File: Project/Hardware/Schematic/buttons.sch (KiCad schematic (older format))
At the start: 0 parts

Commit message: Add files via upload (#6)
Switches inlagda och MicroUSB
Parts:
- added U7, U8: MomentSwitch, PASC:Momentswitch, symbol PASC:MomentSwitch
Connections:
- new net: U8.1 (IN1), U8.2 (IN2)
- new net: U8.3 (OUT1), U8.4 (OUT2)
- new net GND: U7.1 (IN1), U7.2 (IN2)
- new net NRST: U7.3 (OUT1), U7.4 (OUT2)
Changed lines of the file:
@@
 $Descr A4 11693 8268
 encoding utf-8
-Sheet 1 7
+Sheet 7 7
 Title ""
 Date ""
@@
 Comment4 ""
 $EndDescr
+$Comp
+L PASC:MomentSwitch U8
+U 1 1 5C5ECE12
+P 3800 2550
+F 0 "U8" H 3825 2975 50  0000 C CNN
+F 1 "MomentSwitch" H 3825 2884 50  0000 C CNN
+F 2 "PASC:Momentswitch" H 3800 2550 50  0001 C CNN
+F 3 "" H 3800 2550 50  0001 C CNN
+	1    3800 2550
+	1    0    0    -1
+$EndComp
+$Comp
+L PASC:MomentSwitch U7
+U 1 1 5C5ECEC3
+P 3800 1700
+F 0 "U7" H 3825 2125 50  0000 C CNN
+F 1 "MomentSwitch" H 3825 2034 50  0000 C CNN
+F 2 "PASC:Momentswitch" H 3800 1700 50  0001 C CNN
+F 3 "" H 3800 1700 50  0001 C CNN
+	1    3800 1700
+	1    0    0    -1
+$EndComp
+Wire Wire Line
+	3450 1500 3350 1500
+Wire Wire Line
+	3350 1500 3350 1700
+Wire Wire Line
+	3350 1900 3450 1900
+Wire Wire Line
+	3450 2350 3350 2350
+Wire Wire Line
+	3350 2350 3350 2750
+Wire Wire Line
+	3350 2750 3450 2750
+Wire Wire Line
+	4150 1500 4250 1500
+Wire Wire Line
+	4250 1500 4250 1700
+Wire Wire Line
+	4250 1900 4150 1900
+Wire Wire Line
+	4150 2350 4250 2350
+Wire Wire Line
+	4250 2350 4250 2750
+Wire Wire Line
+	4250 2750 4150 2750
+Wire Wire Line
+	4250 1700 4350 1700
+Connection ~ 4250 1700
+Wire Wire Line
+	4250 1700 4250 1900
+Text Label 4350 1700 0    50   ~ 0
+NRST
+Wire Wire Line
+	3350 1700 3250 1700
+Connection ~ 3350 1700
+Wire Wire Line
+	3350 1700 3350 1900
+$Comp
+L power:GND #PWR?
+U 1 1 5C5ED863
+P 3250 1700
+F 0 "#PWR?" H 3250 1450 50  0001 C CNN
+F 1 "GND" H 3255 1527 50  0000 C CNN
+F 2 "" H 3250 1700 50  0001 C CNN
+F 3 "" H 3250 1700 50  0001 C CNN
+	1    3250 1700
+	1    0    0    -1
+$EndComp
 $EndSCHEMATC

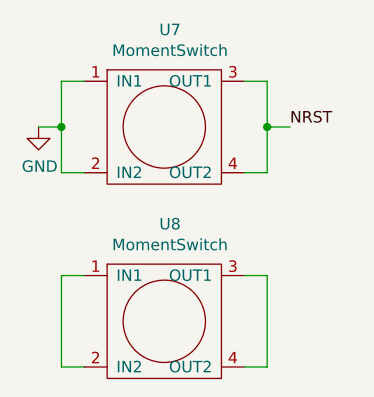
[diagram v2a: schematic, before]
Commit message: Pulse, piezo och labels (#8)
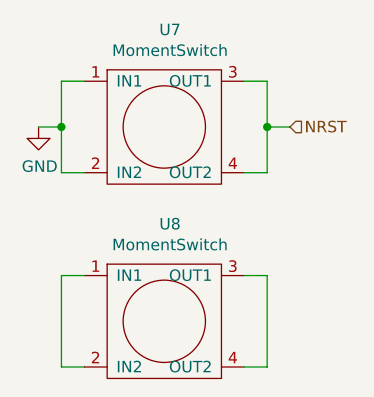
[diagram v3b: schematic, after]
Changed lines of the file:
@@
 Wire Wire Line
 	4250 1700 4250 1900
-Text Label 4350 1700 0    50   ~ 0
-NRST
 Wire Wire Line
 	3350 1700 3250 1700
@@
 	1    0    0    -1
 $EndComp
+Text HLabel 4350 1700 2    50   Input ~ 0
+NRST
 $EndSCHEMATC

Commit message: Buttons och display
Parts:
- added R? (x3): 1k, symbol Device:R
- added U? (x3): MomentSwitch, PASC:Momentswitch, symbol PASC:MomentSwitch
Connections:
- net GND: now also R?.2, R?.2, R?.2
- new net +3V3: U?.1 (IN1), U?.1 (IN1), U?.1 (IN1), U?.2 (IN2), U?.2 (IN2), U?.2 (IN2)
- new net TIM_INC: R?.1, U?.3 (OUT1), U?.4 (OUT2)
- new net TIM_RES: R?.1, U?.3 (OUT1), U?.4 (OUT2)
- new net TIM_START: R?.1, U?.3 (OUT1), U?.4 (OUT2)
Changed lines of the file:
@@
 Text HLabel 4350 1700 2    50   Input ~ 0
 NRST
+$Comp
+L PASC:MomentSwitch U?
+U 1 1 5C68DC82
+P 3800 3500
+F 0 "U?" H 3800 3925 50  0000 C CNN
+F 1 "MomentSwitch" H 3800 3834 50  0000 C CNN
+F 2 "PASC:Momentswitch" H 3800 3500 50  0001 C CNN
+F 3 "" H 3800 3500 50  0001 C CNN
+	1    3800 3500
+	1    0    0    -1
+$EndComp
+Wire Wire Line
+	4150 3300 4250 3300
+Wire Wire Line
+	4250 3700 4150 3700
+Wire Wire Line
+	3450 3300 3350 3300
+Wire Wire Line
+	3350 3700 3450 3700
+Text HLabel 4750 3500 2    50   Input ~ 0
+TIM_START
+Wire Wire Line
+	3350 3300 3350 3500
+$Comp
+L power:+3.3V #PWR?
+U 1 1 5C68E9D0
+P 3150 3400
+F 0 "#PWR?" H 3150 3250 50  0001 C CNN
+F 1 "+3.3V" H 3165 3573 50  0000 C CNN
+F 2 "" H 3150 3400 50  0001 C CNN
+F 3 "" H 3150 3400 50  0001 C CNN
+	1    3150 3400
+	1    0    0    -1
+$EndComp
+Wire Wire Line
+	3150 3400 3150 3500
+Wire Wire Line
+	3150 3500 3350 3500
+Connection ~ 3350 3500
+Wire Wire Line
+	3350 3500 3350 3700
+Wire Wire Line
+	4250 3300 4250 3500
+$Comp
+L Device:R R?
+U 1 1 5C68EFD4
+P 4550 3850
+F 0 "R?" H 4620 3896 50  0000 L CNN
+F 1 "1k" H 4620 3805 50  0000 L CNN
+F 2 "" V 4480 3850 50  0001 C CNN
+F 3 "~" H 4550 3850 50  0001 C CNN
+	1    4550 3850
+	1    0    0    -1
+$EndComp
+Wire Wire Line
+	4250 3500 4550 3500
+Connection ~ 4250 3500
+Wire Wire Line
+	4250 3500 4250 3700
+$Comp
+L power:GND #PWR?
+U 1 1 5C68F32C
+P 4550 4100
+F 0 "#PWR?" H 4550 3850 50  0001 C CNN
+F 1 "GND" H 4555 3927 50  0000 C CNN
+F 2 "" H 4550 4100 50  0001 C CNN
+F 3 "" H 4550 4100 50  0001 C CNN
+	1    4550 4100
+	1    0    0    -1
+$EndComp
+Wire Wire Line
+	4550 4000 4550 4100
+Wire Wire Line
+	4550 3700 4550 3500
+Connection ~ 4550 3500
+Wire Wire Line
+	4550 3500 4750 3500
+$Comp
+L PASC:MomentSwitch U?
+U 1 1 5C68FABB
+P 3800 4850
+F 0 "U?" H 3800 5275 50  0000 C CNN
+F 1 "MomentSwitch" H 3800 5184 50  0000 C CNN
+F 2 "PASC:Momentswitch" H 3800 4850 50  0001 C CNN
+F 3 "" H 3800 4850 50  0001 C CNN
+	1    3800 4850
+	1    0    0    -1
+$EndComp
+Wire Wire Line
+	4150 4650 4250 4650
+Wire Wire Line
+	4250 5050 4150 5050
+Wire Wire Line
+	3450 4650 3350 4650
+Wire Wire Line
+	3350 5050 3450 5050
+Text HLabel 4750 4850 2    50   Input ~ 0
+TIM_INC
+Wire Wire Line
+	3350 4650 3350 4850
+$Comp
+L power:+3.3V #PWR?
+U 1 1 5C68FAC8
+P 3150 4750
+F 0 "#PWR?" H 3150 4600 50  0001 C CNN
+F 1 "+3.3V" H 3165 4923 50  0000 C CNN
+F 2 "" H 3150 4750 50  0001 C CNN
+F 3 "" H 3150 4750 50  0001 C CNN
+	1    3150 4750
+	1    0    0    -1
+$EndComp
+Wire Wire Line
+	3150 4750 3150 4850
+Wire Wire Line
+	3150 4850 3350 4850
+Connection ~ 3350 4850
+Wire Wire Line
+	3350 4850 3350 5050
+Wire Wire Line
+	4250 4650 4250 4850
+$Comp
+L Device:R R?
+U 1 1 5C68FAD3
+P 4550 5200
+F 0 "R?" H 4620 5246 50  0000 L CNN
+F 1 "1k" H 4620 5155 50  0000 L CNN
+F 2 "" V 4480 5200 50  0001 C CNN
+F 3 "~" H 4550 5200 50  0001 C CNN
+	1    4550 5200
+	1    0    0    -1
+$EndComp
+Wire Wire Line
+	4250 4850 4550 4850
+Connection ~ 4250 4850
+Wire Wire Line
+	4250 4850 4250 5050
+$Comp
+L power:GND #PWR?
+U 1 1 5C68FADD
+P 4550 5450
+F 0 "#PWR?" H 4550 5200 50  0001 C CNN
+F 1 "GND" H 4555 5277 50  0000 C CNN
+F 2 "" H 4550 5450 50  0001 C CNN
+F 3 "" H 4550 5450 50  0001 C CNN
+	1    4550 5450
+	1    0    0    -1
+$EndComp
+Wire Wire Line
+	4550 5350 4550 5450
+Wire Wire Line
+	4550 5050 4550 4850
+Connection ~ 4550 4850
+Wire Wire Line
+	4550 4850 4750 4850
+$Comp
+L PASC:MomentSwitch U?
+U 1 1 5C6902F1
+P 3800 6050
+F 0 "U?" H 3800 6475 50  0000 C CNN
+F 1 "MomentSwitch" H 3800 6384 50  0000 C CNN
+F 2 "PASC:Momentswitch" H 3800 6050 50  0001 C CNN
+F 3 "" H 3800 6050 50  0001 C CNN
+	1    3800 6050
+	1    0    0    -1
+$EndComp
+Wire Wire Line
+	4150 5850 4250 5850
+Wire Wire Line
+	4250 6250 4150 6250
+Wire Wire Line
+	3450 5850 3350 5850
+Wire Wire Line
+	3350 6250 3450 6250
+Text HLabel 4750 6050 2    50   Input ~ 0
+TIM_RES
+Wire Wire Line
+	3350 5850 3350 6050
+$Comp
+L power:+3.3V #PWR?
+U 1 1 5C6902FE
+P 3150 5950
+F 0 "#PWR?" H 3150 5800 50  0001 C CNN
+F 1 "+3.3V" H 3165 6123 50  0000 C CNN
+F 2 "" H 3150 5950 50  0001 C CNN
+F 3 "" H 3150 5950 50  0001 C CNN
+	1    3150 5950
+	1    0    0    -1
+$EndComp
+Wire Wire Line
+	3150 5950 3150 6050
+Wire Wire Line
+	3150 6050 3350 6050
+Connection ~ 3350 6050
+Wire Wire Line
+	3350 6050 3350 6250
+Wire Wire Line
+	4250 5850 4250 6050
+$Comp
+L Device:R R?
+U 1 1 5C690309
+P 4550 6400
+F 0 "R?" H 4620 6446 50  0000 L CNN
+F 1 "1k" H 4620 6355 50  0000 L CNN
+F 2 "" V 4480 6400 50  0001 C CNN
+F 3 "~" H 4550 6400 50  0001 C CNN
+	1    4550 6400
+	1    0    0    -1
+$EndComp
+Wire Wire Line
+	4250 6050 4550 6050
+Connection ~ 4250 6050
+Wire Wire Line
+	4250 6050 4250 6250
+$Comp
+L power:GND #PWR?
+U 1 1 5C690313
+P 4550 6650
+F 0 "#PWR?" H 4550 6400 50  0001 C CNN
+F 1 "GND" H 4555 6477 50  0000 C CNN
+F 2 "" H 4550 6650 50  0001 C CNN
+F 3 "" H 4550 6650 50  0001 C CNN
+	1    4550 6650
+	1    0    0    -1
+$EndComp
+Wire Wire Line
+	4550 6550 4550 6650
+Wire Wire Line
+	4550 6250 4550 6050
+Connection ~ 4550 6050
+Wire Wire Line
+	4550 6050 4750 6050
 $EndSCHEMATC

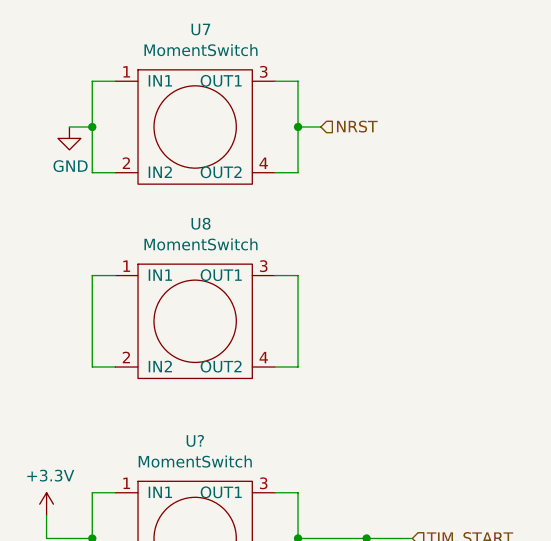
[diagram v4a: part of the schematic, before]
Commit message: Tagit bort knapp, ändrat power till piezo
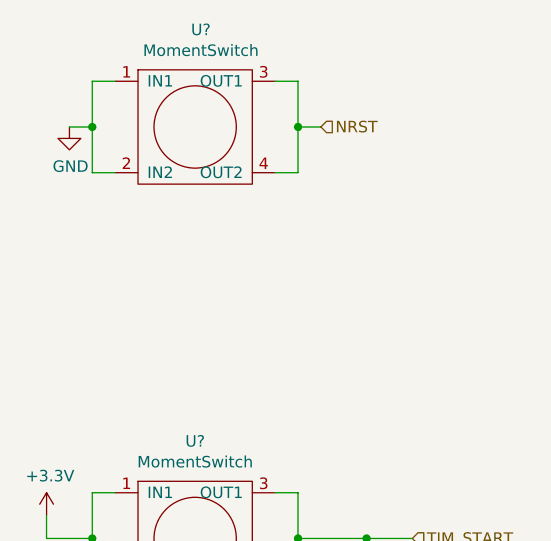
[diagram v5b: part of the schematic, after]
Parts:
- removed U8: MomentSwitch, PASC:Momentswitch, symbol PASC:MomentSwitch
- renumbered U7 to U?
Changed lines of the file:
@@
 $EndDescr
 $Comp
-L PASC:MomentSwitch U8
-U 1 1 5C5ECE12
-P 3800 2550
-F 0 "U8" H 3825 2975 50  0000 C CNN
-F 1 "MomentSwitch" H 3825 2884 50  0000 C CNN
-F 2 "PASC:Momentswitch" H 3800 2550 50  0001 C CNN
-F 3 "" H 3800 2550 50  0001 C CNN
-	1    3800 2550
-	1    0    0    -1
-$EndComp
-$Comp
-L PASC:MomentSwitch U7
+L PASC:MomentSwitch U?
 U 1 1 5C5ECEC3
 P 3800 1700
-F 0 "U7" H 3825 2125 50  0000 C CNN
+F 0 "U?" H 3825 2125 50  0000 C CNN
 F 1 "MomentSwitch" H 3825 2034 50  0000 C CNN
 F 2 "PASC:Momentswitch" H 3800 1700 50  0001 C CNN
@@
 	3350 1900 3450 1900
 Wire Wire Line
-	3450 2350 3350 2350
-Wire Wire Line
-	3350 2350 3350 2750
-Wire Wire Line
-	3350 2750 3450 2750
-Wire Wire Line
 	4150 1500 4250 1500
 Wire Wire Line
@@
 	4250 1900 4150 1900
 Wire Wire Line
-	4150 2350 4250 2350
-Wire Wire Line
-	4250 2350 4250 2750
-Wire Wire Line
-	4250 2750 4150 2750
-Wire Wire Line
 	4250 1700 4350 1700

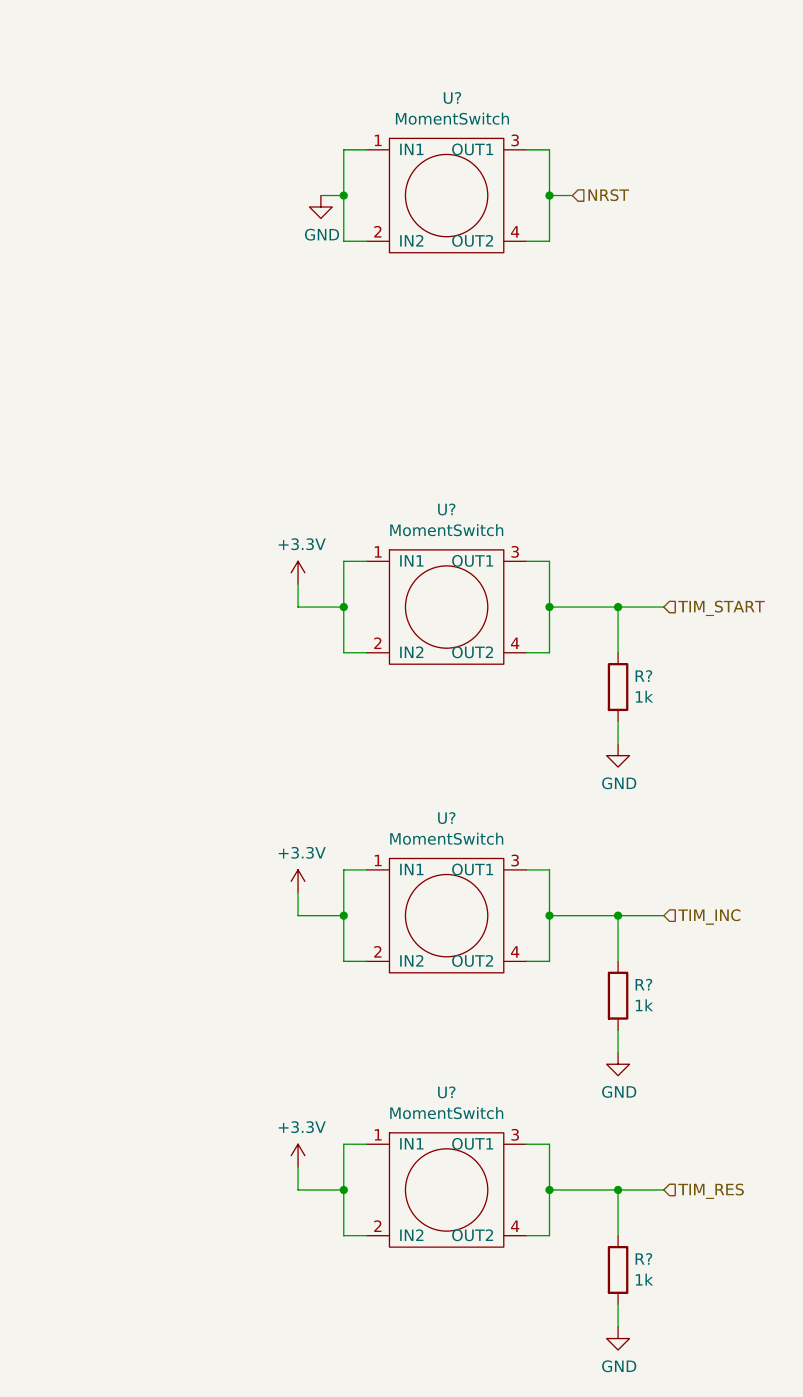
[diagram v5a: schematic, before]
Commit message: Tog bort power supply +7, lade till switch för att switcha mellan batteri och USB power. Lade till power-net symbol för oregulerad supply voltage +VIN.
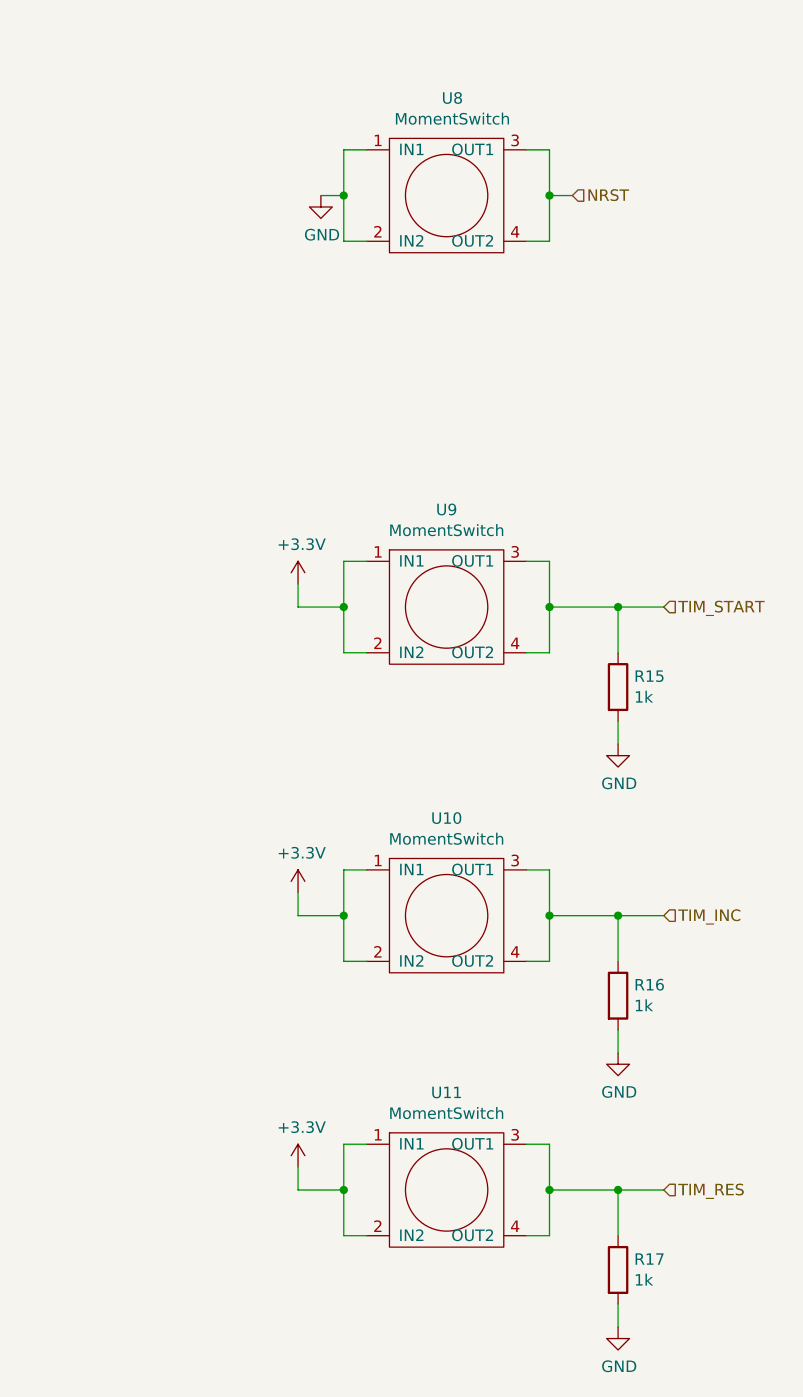
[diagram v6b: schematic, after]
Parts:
- gave numbers to parts that had none: 7
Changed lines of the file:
@@
 $EndDescr
 $Comp
-L PASC:MomentSwitch U?
+L PASC:MomentSwitch U8
 U 1 1 5C5ECEC3
 P 3800 1700
-F 0 "U?" H 3825 2125 50  0000 C CNN
+F 0 "U8" H 3825 2125 50  0000 C CNN
 F 1 "MomentSwitch" H 3825 2034 50  0000 C CNN
 F 2 "PASC:Momentswitch" H 3800 1700 50  0001 C CNN
@@
 	3350 1700 3350 1900
 $Comp
-L power:GND #PWR?
+L power:GND #PWR0139
 U 1 1 5C5ED863
 P 3250 1700
-F 0 "#PWR?" H 3250 1450 50  0001 C CNN
+F 0 "#PWR0139" H 3250 1450 50  0001 C CNN
 F 1 "GND" H 3255 1527 50  0000 C CNN
 F 2 "" H 3250 1700 50  0001 C CNN
@@
 NRST
 $Comp
-L PASC:MomentSwitch U?
+L PASC:MomentSwitch U9
 U 1 1 5C68DC82
 P 3800 3500
-F 0 "U?" H 3800 3925 50  0000 C CNN
+F 0 "U9" H 3800 3925 50  0000 C CNN
 F 1 "MomentSwitch" H 3800 3834 50  0000 C CNN
 F 2 "PASC:Momentswitch" H 3800 3500 50  0001 C CNN
@@
 	3350 3300 3350 3500
 $Comp
-L power:+3.3V #PWR?
+L power:+3.3V #PWR0140
 U 1 1 5C68E9D0
 P 3150 3400
-F 0 "#PWR?" H 3150 3250 50  0001 C CNN
+F 0 "#PWR0140" H 3150 3250 50  0001 C CNN
 F 1 "+3.3V" H 3165 3573 50  0000 C CNN
 F 2 "" H 3150 3400 50  0001 C CNN
@@
 	4250 3300 4250 3500
 $Comp
-L Device:R R?
+L Device:R R15
 U 1 1 5C68EFD4
 P 4550 3850
-F 0 "R?" H 4620 3896 50  0000 L CNN
+F 0 "R15" H 4620 3896 50  0000 L CNN
 F 1 "1k" H 4620 3805 50  0000 L CNN
 F 2 "" V 4480 3850 50  0001 C CNN
@@
 	4250 3500 4250 3700
 $Comp
-L power:GND #PWR?
+L power:GND #PWR0141
 U 1 1 5C68F32C
 P 4550 4100
-F 0 "#PWR?" H 4550 3850 50  0001 C CNN
+F 0 "#PWR0141" H 4550 3850 50  0001 C CNN
 F 1 "GND" H 4555 3927 50  0000 C CNN
 F 2 "" H 4550 4100 50  0001 C CNN
@@
 	4550 3500 4750 3500
 $Comp
-L PASC:MomentSwitch U?
+L PASC:MomentSwitch U10
 U 1 1 5C68FABB
 P 3800 4850
-F 0 "U?" H 3800 5275 50  0000 C CNN
+F 0 "U10" H 3800 5275 50  0000 C CNN
 F 1 "MomentSwitch" H 3800 5184 50  0000 C CNN
 F 2 "PASC:Momentswitch" H 3800 4850 50  0001 C CNN
@@
 	3350 4650 3350 4850
 $Comp
-L power:+3.3V #PWR?
+L power:+3.3V #PWR0142
 U 1 1 5C68FAC8
 P 3150 4750
-F 0 "#PWR?" H 3150 4600 50  0001 C CNN
+F 0 "#PWR0142" H 3150 4600 50  0001 C CNN
 F 1 "+3.3V" H 3165 4923 50  0000 C CNN
 F 2 "" H 3150 4750 50  0001 C CNN
@@
 	4250 4650 4250 4850
 $Comp
-L Device:R R?
+L Device:R R16
 U 1 1 5C68FAD3
 P 4550 5200
-F 0 "R?" H 4620 5246 50  0000 L CNN
+F 0 "R16" H 4620 5246 50  0000 L CNN
 F 1 "1k" H 4620 5155 50  0000 L CNN
 F 2 "" V 4480 5200 50  0001 C CNN
@@
 	4250 4850 4250 5050
 $Comp
-L power:GND #PWR?
+L power:GND #PWR0143
 U 1 1 5C68FADD
 P 4550 5450
-F 0 "#PWR?" H 4550 5200 50  0001 C CNN
+F 0 "#PWR0143" H 4550 5200 50  0001 C CNN
 F 1 "GND" H 4555 5277 50  0000 C CNN
 F 2 "" H 4550 5450 50  0001 C CNN
@@
 	4550 4850 4750 4850
 $Comp
-L PASC:MomentSwitch U?
+L PASC:MomentSwitch U11
 U 1 1 5C6902F1
 P 3800 6050
-F 0 "U?" H 3800 6475 50  0000 C CNN
+F 0 "U11" H 3800 6475 50  0000 C CNN
 F 1 "MomentSwitch" H 3800 6384 50  0000 C CNN
 F 2 "PASC:Momentswitch" H 3800 6050 50  0001 C CNN
@@
 	3350 5850 3350 6050
 $Comp
-L power:+3.3V #PWR?
+L power:+3.3V #PWR0144
 U 1 1 5C6902FE
 P 3150 5950
-F 0 "#PWR?" H 3150 5800 50  0001 C CNN
+F 0 "#PWR0144" H 3150 5800 50  0001 C CNN
 F 1 "+3.3V" H 3165 6123 50  0000 C CNN
 F 2 "" H 3150 5950 50  0001 C CNN
@@
 	4250 5850 4250 6050
 $Comp
-L Device:R R?
+L Device:R R17
 U 1 1 5C690309
 P 4550 6400
-F 0 "R?" H 4620 6446 50  0000 L CNN
+F 0 "R17" H 4620 6446 50  0000 L CNN
 F 1 "1k" H 4620 6355 50  0000 L CNN
 F 2 "" V 4480 6400 50  0001 C CNN
@@
 	4250 6050 4250 6250
 $Comp
-L power:GND #PWR?
+L power:GND #PWR0145
 U 1 1 5C690313
 P 4550 6650
-F 0 "#PWR?" H 4550 6400 50  0001 C CNN
+F 0 "#PWR0145" H 4550 6400 50  0001 C CNN
 F 1 "GND" H 4555 6477 50  0000 C CNN
 F 2 "" H 4550 6650 50  0001 C CNN

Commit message: Intermediate...
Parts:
- R15, R16, R17: footprint (none) -> Resistor_SMD:R_0805_2012Metric_Pad1.15x1.40mm_HandSolder
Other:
- moved on the sheet: R15, R16, R17, U10, U11, U8, U9
